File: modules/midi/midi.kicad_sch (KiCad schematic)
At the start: 17 parts, among them J1 MIDI_IN, U1 ATtiny1616-M

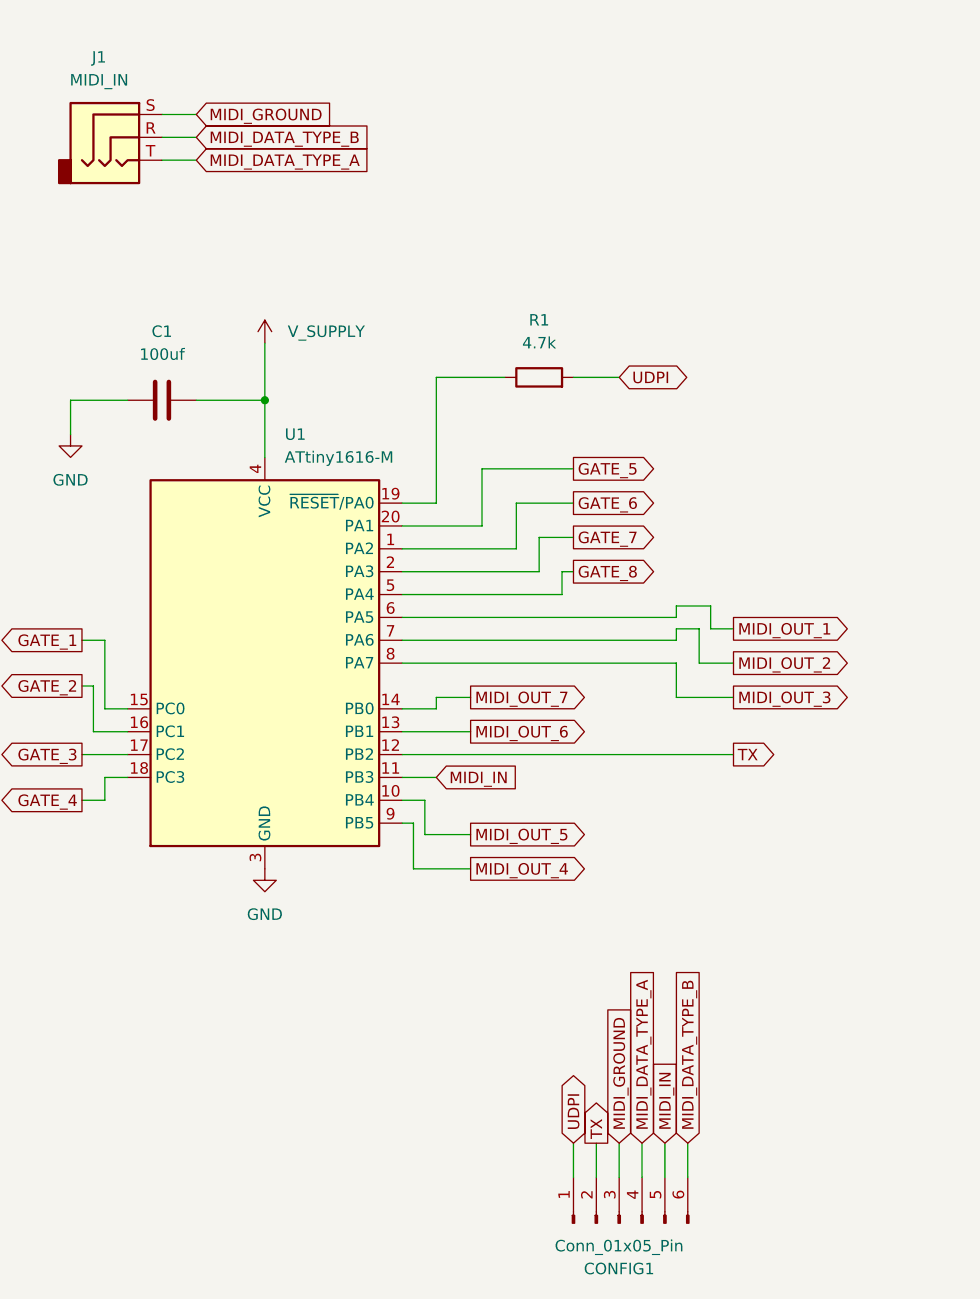
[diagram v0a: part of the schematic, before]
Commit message: midi: Connect MIDI ground to common GND
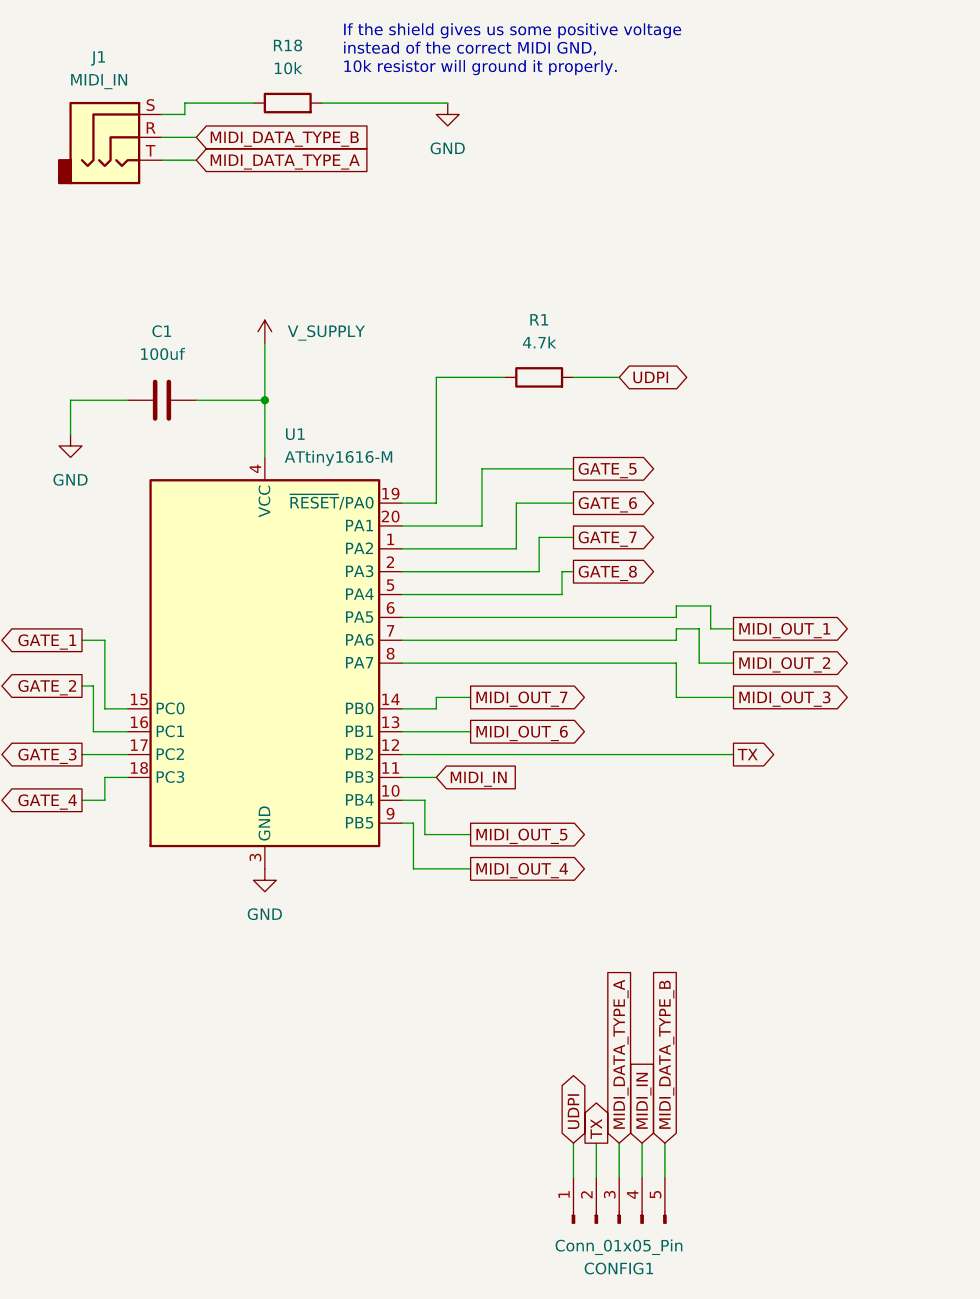
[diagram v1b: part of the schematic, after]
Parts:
- added R18: 10k, Resistor_SMD:R_0402_1005Metric, symbol Device:R
- CONFIG1: footprint BreadModular_MISC:Conn_Holes_6 -> BreadModular_MISC:Power_Connector; symbol Connector:Conn_01x06_Pin -> Connector:Conn_01x05_Pin
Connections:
- net GND: now also R18.2
- net MIDI_DATA_TYPE_A: now also CONFIG1.3 (Pin_3); no longer CONFIG1.4 (Pin_4)
- net MIDI_DATA_TYPE_B: now also CONFIG1.5 (Pin_5); no longer CONFIG1.6 (Pin_6)
- net MIDI_IN: now also CONFIG1.4 (Pin_4); no longer CONFIG1.5 (Pin_5)
- net MIDI_GROUND: no longer names the net of J1.S
- net MIDI_GROUND: now also R18.1; no longer CONFIG1.3 (Pin_3)
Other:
- note added: "If the shield gives us some positive voltage instead of the correct MIDI GND, 10k resistor will ground it properly."

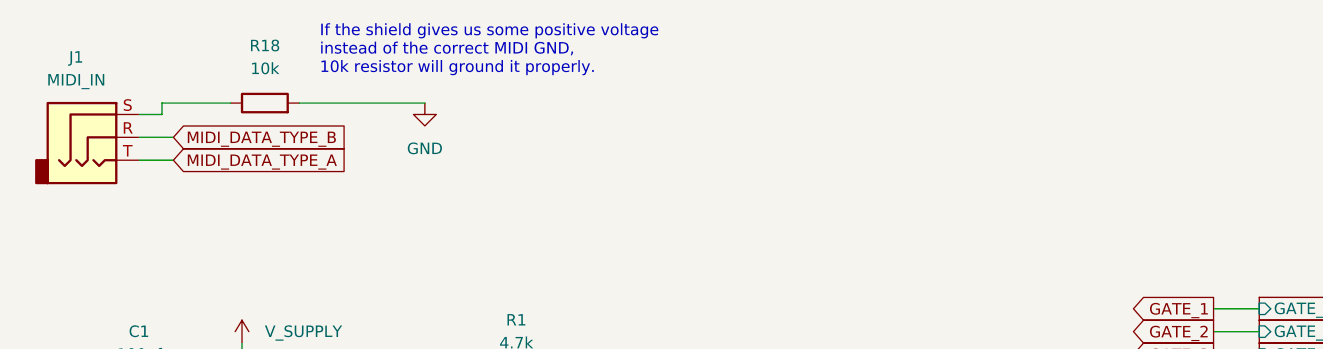
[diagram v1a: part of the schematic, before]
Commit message: midi: fix instability in MIDI recieving
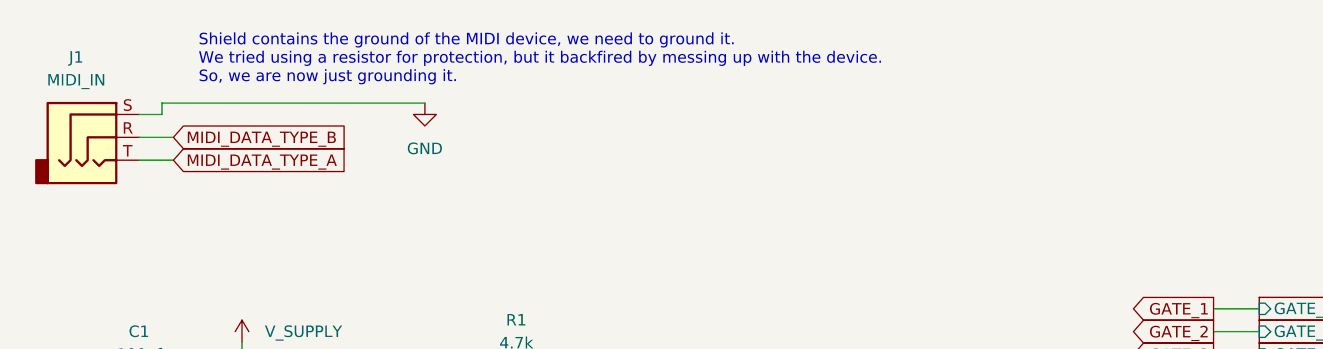
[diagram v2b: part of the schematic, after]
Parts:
- removed R18: 10k, Resistor_SMD:R_0402_1005Metric, symbol Device:R
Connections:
- net GND: now also J1.S
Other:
- note added: "Shield contains the ground of the MIDI device, we need to ground it. We tried using a resistor for protection, but it backfired by messing up with the device. So, we are now just grounding it."
- note removed: "If the shield gives us some positive voltage instead of the correct MIDI GND, 10k resistor will ground it properly."
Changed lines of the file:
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@@
 	(wire
 		(pts
-			(xy 35.56 24.13) (xy 43.18 24.13)
+			(xy 35.56 24.13) (xy 64.77 24.13)
 		)
 		(stroke
@@
 	(wire
 		(pts
-			(xy 50.8 24.13) (xy 64.77 24.13)
-		)
-		(stroke
-			(width 0)
-			(type default)
-		)
-	)
-	(wire
-		(pts
 			(xy 88.9 139.7) (xy 88.9 143.51)
 		)
@@
 		)
 	)
-	(text "If the shield gives us some positive voltage \ninstead of the correct MIDI GND, \n10k resistor will ground it properly."
+	(text "Shield contains the ground of the MIDI device, we need to ground it.\nWe tried using a resistor for protection, but it backfired by messing up with the device.\nSo, we are now just grounding it."
 		(exclude_from_sim no)
-		(at 53.086 18.288 0)
+		(at 39.624 19.304 0)
 		(effects
 			(font
@@
 					(unit 1)
 				)
-			)
-		)
-	)
-	(symbol
-		(lib_id "Device:R")
-		(at 46.99 24.13 90)
-		(unit 1)
-		(exclude_from_sim no)
-		(in_bom yes)
-		(on_board yes)
-		(dnp no)
-		(fields_autoplaced yes)
-		(property "Reference" "R18"
-			(at 46.99 17.78 90)
-			(effects
-				(font
-					(size 1.27 1.27)
-				)
-			)
-		)
-		(property "Value" "10k"
-			(at 46.99 20.32 90)
-			(effects
-				(font
-					(size 1.27 1.27)
-				)
-			)
-		)
-		(property "Footprint" "Resistor_SMD:R_0402_1005Metric"
-			(at 46.99 25.908 90)
-			(effects
-				(font
-					(size 1.27 1.27)
-				)
-				(hide yes)
-			)
-		)
-		(property "Datasheet" "~"
-			(at 46.99 24.13 0)
-			(effects
-				(font
-					(size 1.27 1.27)
-				)
-				(hide yes)
-			)
-		)
-		(property "Description" "Resistor"
-			(at 46.99 24.13 0)
-			(effects
-				(font
-					(size 1.27 1.27)
-				)
-				(hide yes)
-			)
-		)
-		(pin "2"
-		)
-		(pin "1"
-		)
-		(instances
-			(project "midi"
-				(path "/b63493d3-5f6d-47e3-845b-87e7090fc1ab"
-					(reference "R18")
-					(unit 1)
-				)

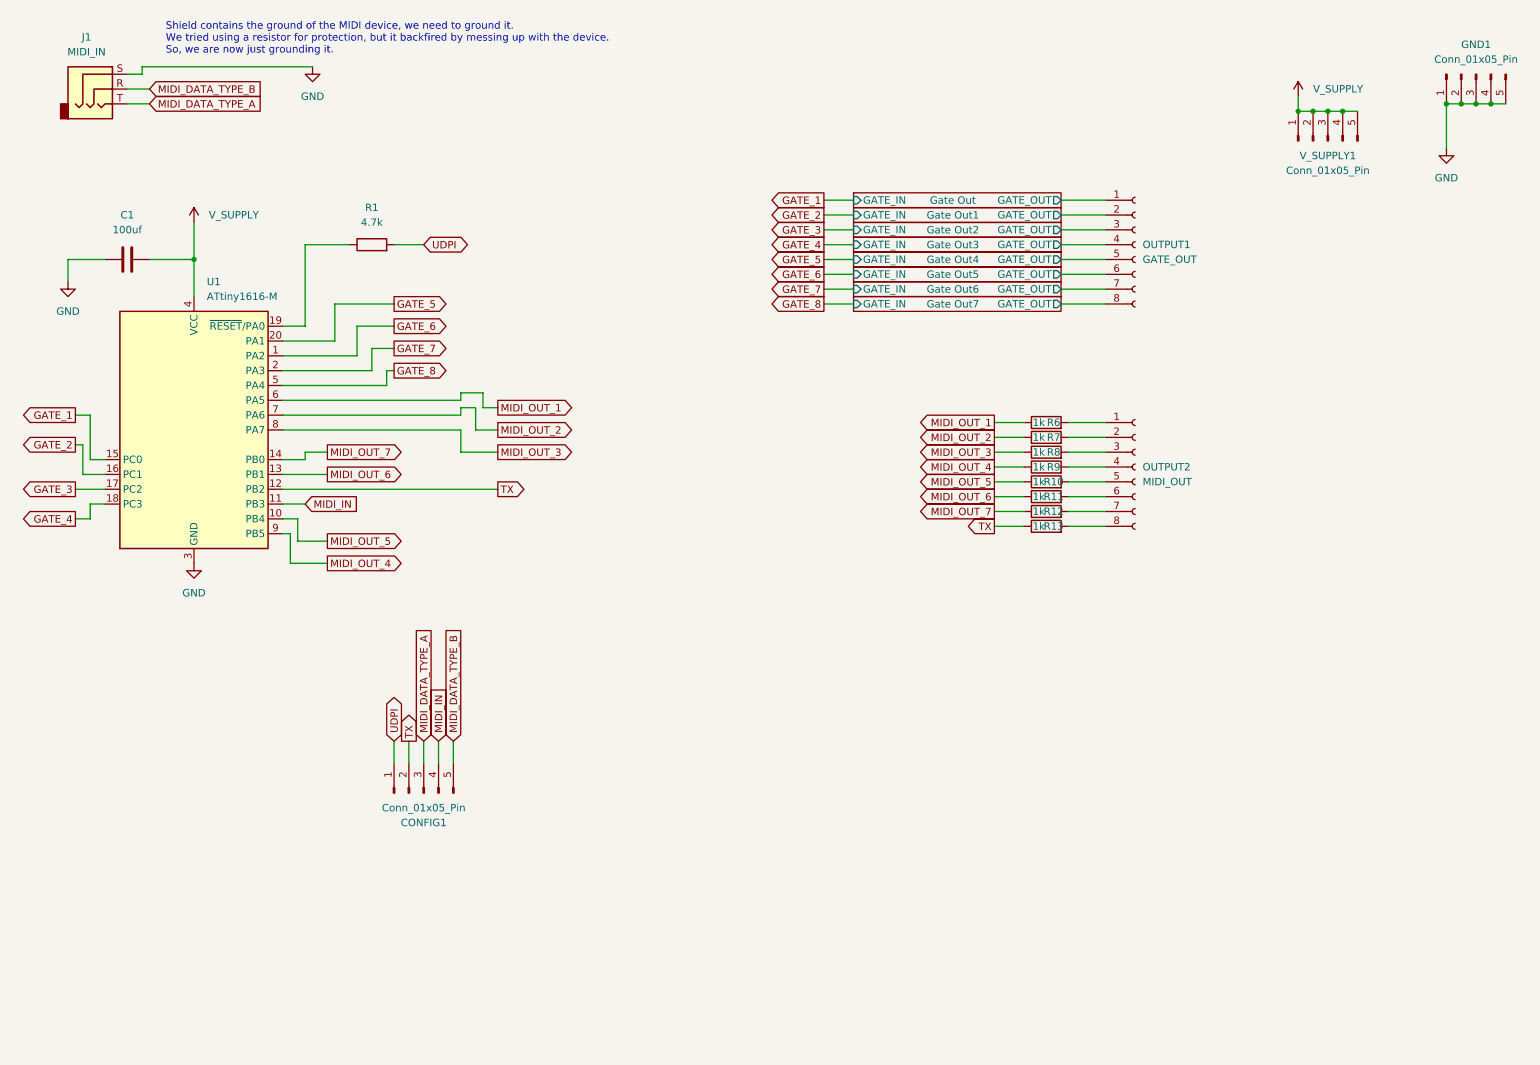
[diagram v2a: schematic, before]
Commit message: Add opto-couplers for the midi input
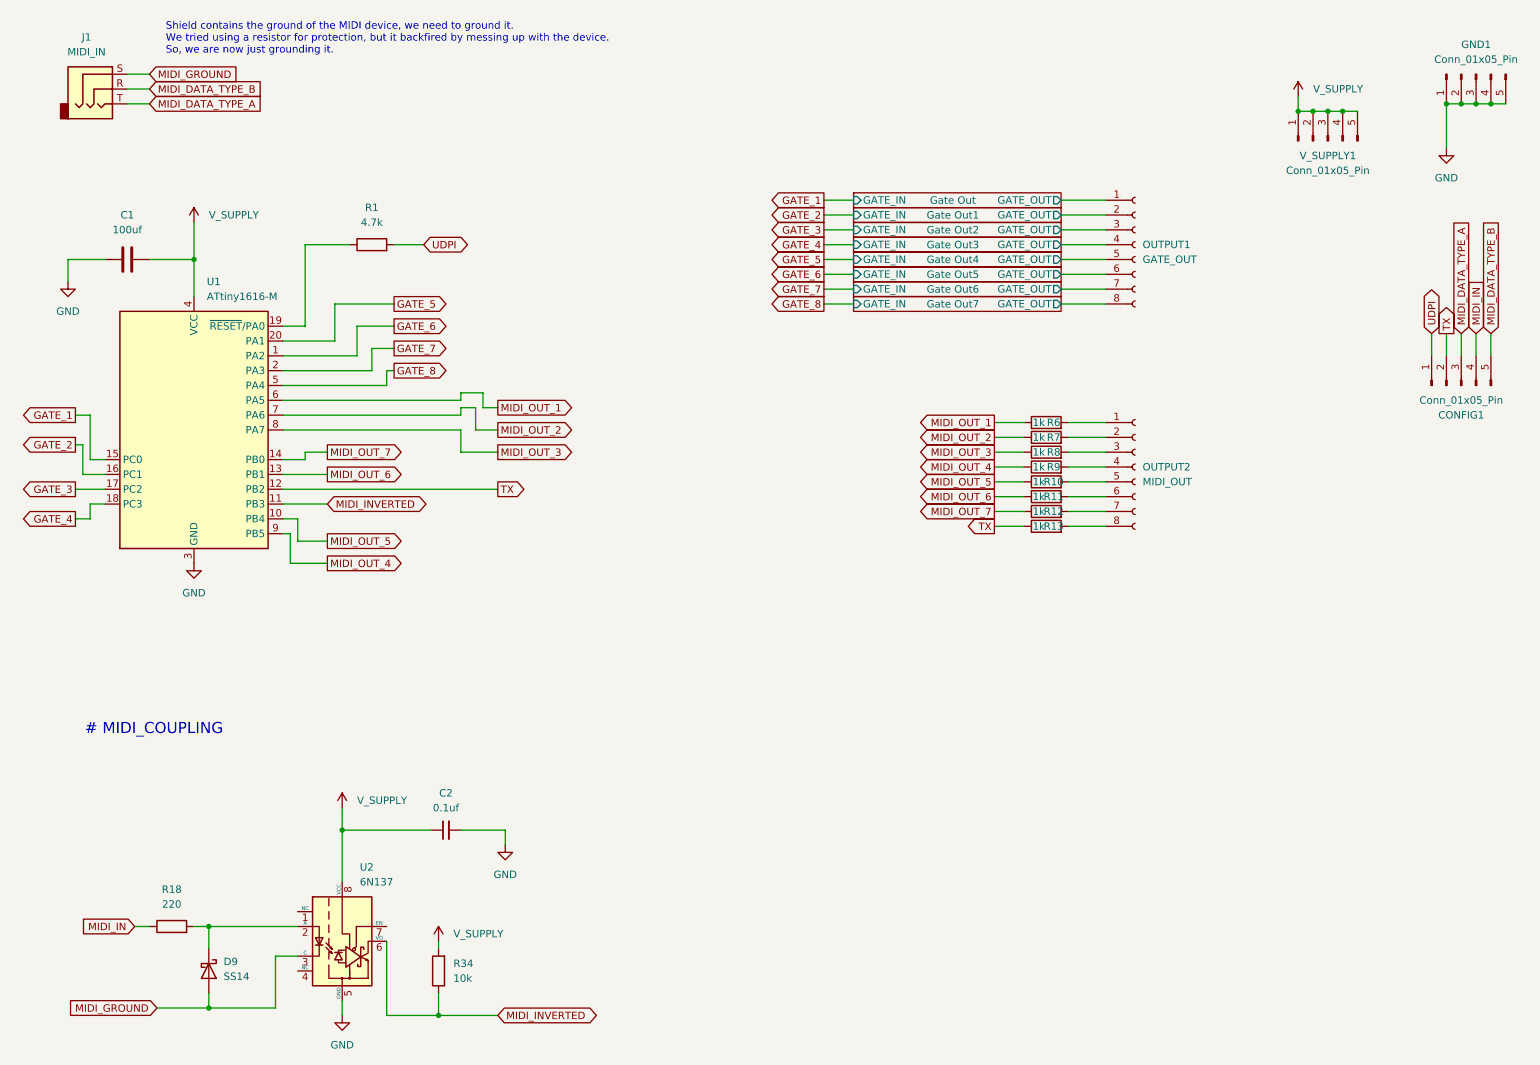
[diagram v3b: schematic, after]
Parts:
- added C2: 0.1uf, Capacitor_SMD:C_0402_1005Metric, symbol Device:C_Small
- added D9: SS14, Diode_SMD:D_SMA, symbol Diode:SS14
- added R18: 220, Resistor_SMD:R_0402_1005Metric, symbol Device:R
- added R34: 10k, Resistor_SMD:R_0402_1005Metric, symbol Device:R
- added U2: 6N137, BreadModular_MISC:SOIC-8 2.54, symbol Isolator:6N137
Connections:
- net GND: now also C2.2, U2.5 (GND); no longer J1.S
- net MIDI_IN: now also R18.1; no longer U1.11 (PB3)
- net V_SUPPLY: now also C2.1, R34.2, U2.8 (VCC)
- new net: D9.1 (K), R18.2, U2.2 (A)
- new net MIDI_GROUND: D9.2 (A), J1.S, U2.3 (C)
- new net MIDI_INVERTED: R34.1, U1.11 (PB3), U2.6 (VO)
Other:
- note added: "# MIDI_COUPLING"
- moved on the sheet: CONFIG1
